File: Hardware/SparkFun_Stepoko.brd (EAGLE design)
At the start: 150 x 82 mm, 184 parts, among them J1 AVR ISP, Q1 16MHZ, Q2 100A/100V, U1 ATMEGA328, U2 CY7C65213, U3 74LVC1G04, U4 LM25011, U5 DRV8811, U6 74HC7014D, U7 7432SE, U8 DRV8811, U9 DRV8811

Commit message: found via hitting trace
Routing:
- net 5V: track 615.3 -> 613.5 mm
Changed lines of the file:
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@@
 <vertex x="15.24" y="37.084"/>
 </polygon>
-<via x="24.172" y="37.814" extent="1-16" drill="0.508" diameter="0.254"/>
-<via x="25.315" y="37.814" extent="1-16" drill="0.508" diameter="0.254"/>
+<via x="26.204" y="37.052" extent="1-16" drill="0.508" diameter="0.254"/>
+<via x="25.569" y="38.068" extent="1-16" drill="0.508" diameter="0.254"/>
 <via x="41.656" y="58.039" extent="1-16" drill="0.508"/>
 <via x="42.672" y="58.039" extent="1-16" drill="0.508"/>
@@
 <vertex x="101" y="78.73"/>
 </polygon>
-<wire x1="125" y1="39" x2="133" y2="39" width="0.4064" layer="16"/>
-<wire x1="133" y1="39" x2="135" y2="39" width="0.4064" layer="16"/>
-<via x="135" y="39" extent="1-16" drill="0.508" diameter="0.254"/>
-<via x="133" y="39" extent="1-16" drill="0.508" diameter="0.254"/>
+<wire x1="125" y1="39" x2="131.984" y2="39" width="0.4064" layer="16"/>
+<wire x1="131.984" y1="39" x2="133.222" y2="39" width="0.4064" layer="16"/>
+<via x="133.222" y="39" extent="1-16" drill="0.508" diameter="0.254"/>
+<via x="131.984" y="39" extent="1-16" drill="0.508" diameter="0.254"/>
 <wire x1="125" y1="30.826" x2="125" y2="36.068" width="0.4064" layer="16"/>
 <contactref element="C50" pad="2"/>

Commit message: corrected issues in github
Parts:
- D10, D14, D6: value YELLOW -> Yellow
- U10: value (none) -> +12v
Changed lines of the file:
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@@
 <layer number="113" name="IDFDebug" color="4" fill="1" visible="yes" active="yes"/>
 <layer number="116" name="Patch_BOT" color="9" fill="4" visible="yes" active="yes"/>
+<layer number="118" name="Rect_Pads" color="7" fill="1" visible="yes" active="yes"/>
 <layer number="121" name="_tsilk" color="7" fill="1" visible="yes" active="yes"/>
 <layer number="122" name="_bsilk" color="7" fill="1" visible="yes" active="yes"/>
@@
 <attribute name="PROD_ID" value="DIO-09912" x="21.5" y="76" size="1.778" layer="27" rot="R90" display="off"/>
 </element>
-<element name="D6" library="SparkFun-LED" package="LED-1206" value="YELLOW" x="29.5" y="76" rot="R90">
+<element name="D6" library="SparkFun-LED" package="LED-1206" value="Yellow" x="29.5" y="76" rot="R90">
 <attribute name="PROD_ID" value="DIO-09909" x="29.5" y="76" size="1.778" layer="27" rot="R90" display="off"/>
 </element>
@@
 <attribute name="PROD_ID" value="DIO-09912" x="40.08" y="70.92" size="1.778" layer="27" rot="R90" display="off"/>
 </element>
-<element name="D10" library="SparkFun-LED" package="LED-1206" value="YELLOW" x="43" y="76" rot="R90">
+<element name="D10" library="SparkFun-LED" package="LED-1206" value="Yellow" x="43" y="76" rot="R90">
 <attribute name="PROD_ID" value="DIO-09909" x="48.08" y="76" size="1.778" layer="27" rot="R90" display="off"/>
 </element>
@@
 <attribute name="PROD_ID" value="DIO-09912" x="53.58" y="70.92" size="1.778" layer="27" rot="R90" display="off"/>
 </element>
-<element name="D14" library="SparkFun-LED" package="LED-1206" value="YELLOW" x="56.5" y="76" rot="R90">
+<element name="D14" library="SparkFun-LED" package="LED-1206" value="Yellow" x="56.5" y="76" rot="R90">
 <attribute name="PROD_ID" value="DIO-09909" x="61.58" y="76" size="1.778" layer="27" rot="R90" display="off"/>
 </element>
@@
 <attribute name="PROD_ID" value="CAP-10547" x="113" y="59.5" size="1.016" layer="27" font="vector" ratio="15" rot="R180" display="off"/>
 </element>
-<element name="U10" library="SparkFun-PowerIC" package="TO-252" value="" x="78" y="67" rot="R90">
+<element name="U10" library="SparkFun-PowerIC" package="TO-252" value="+12v" x="78" y="67" rot="R90">
 <attribute name="PROD_ID" value="VREG-12370" x="78" y="67" size="1.778" layer="27" rot="R90" display="off"/>
 <attribute name="VALUE" value="+12v" x="78" y="67" size="1.778" layer="27" rot="R90" display="off"/>

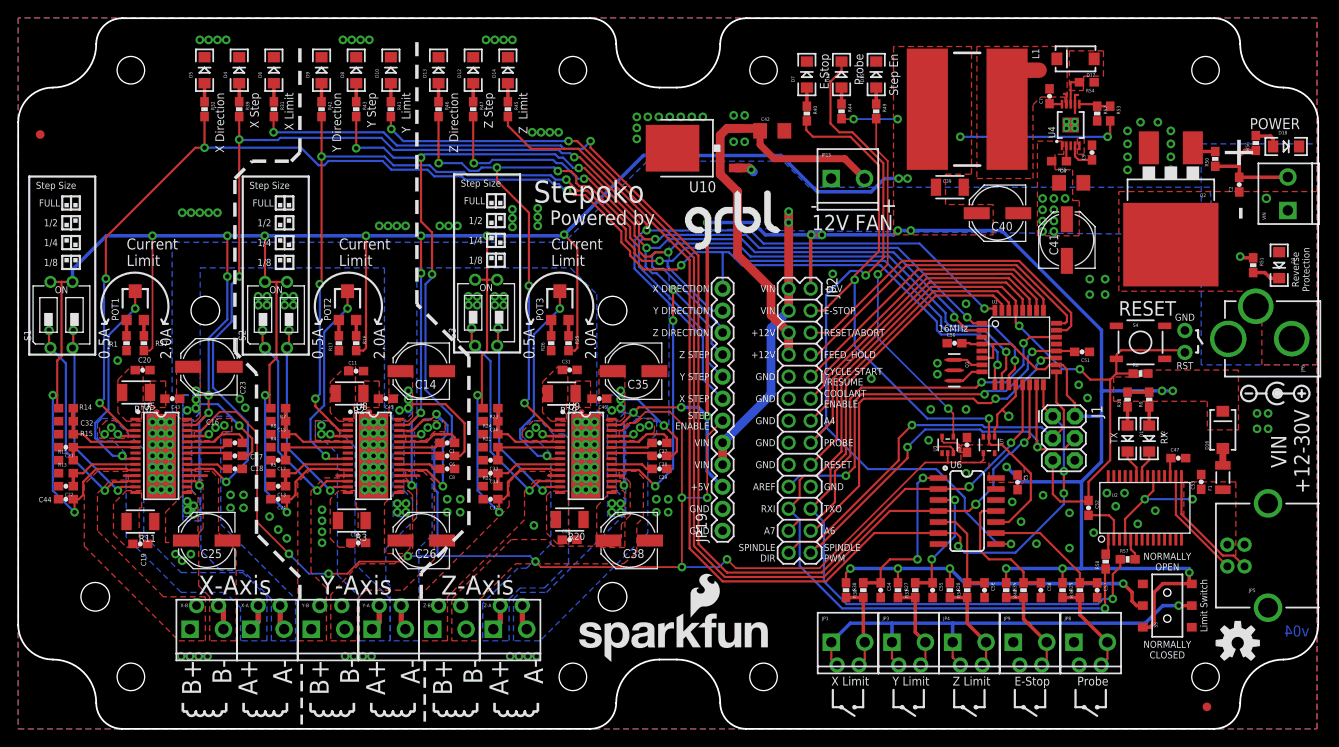
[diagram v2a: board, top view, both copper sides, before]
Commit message: Corrected Probe functionality and updated silk to better reflect limit switch functionality, moved Arduino table to better fit board layout
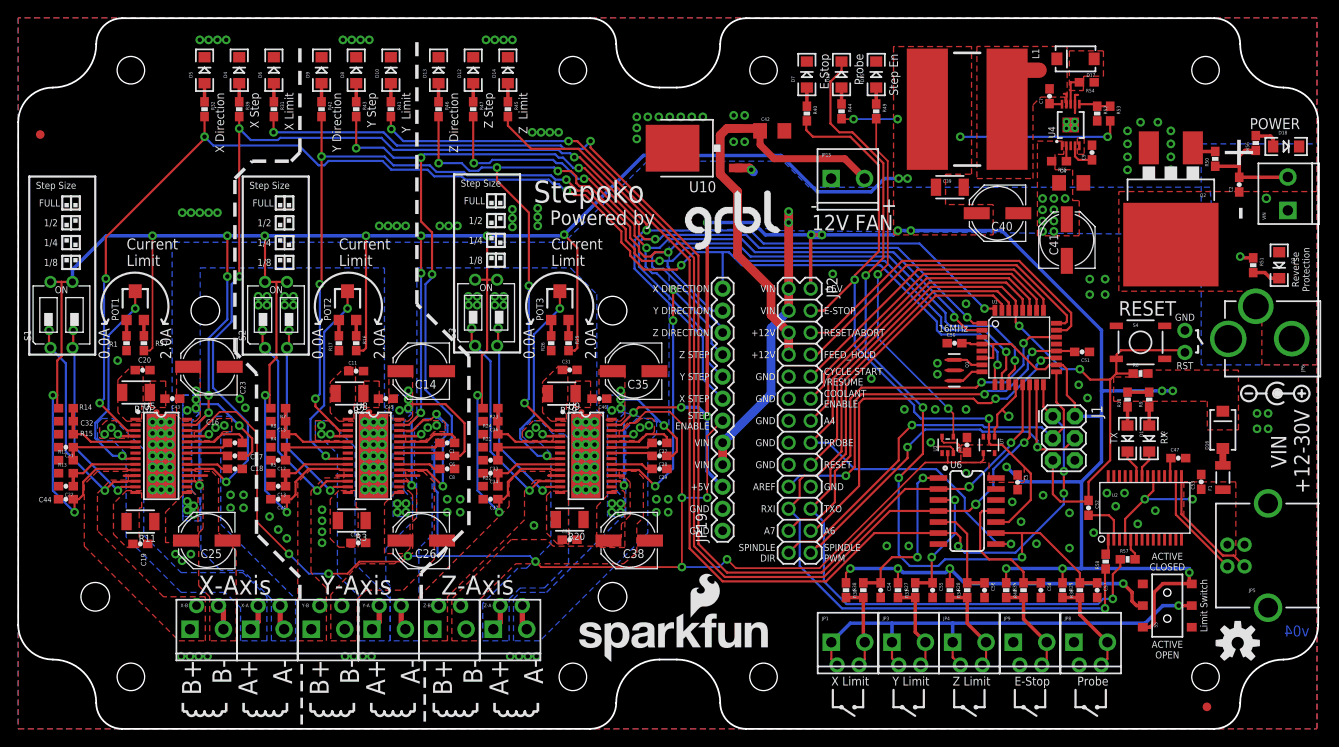
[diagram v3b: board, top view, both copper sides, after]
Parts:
- U2: value CY7C65213 -> FT232RLSSOP
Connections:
- net A5-PROBE: no longer D11.C
- net PROBE: now also D11.C
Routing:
- net PROBE: track 14.7 -> 98.3 mm, vias 0 -> 4
- net A5-PROBE: track 119.7 -> 67.6 mm, vias 2 -> 1
- net D2-STEP-X: track 171.7 -> 172.3 mm
- net GND: vias 149 -> 152
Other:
- board text added: "0.0A"
- board text added: "ACTIVE CLOSED"
- board text added: "ACTIVE OPEN"
- board text removed: "0.5A"
- board text removed: "NORMALLY CLOSED"
- board text removed: "NORMALLY OPEN"

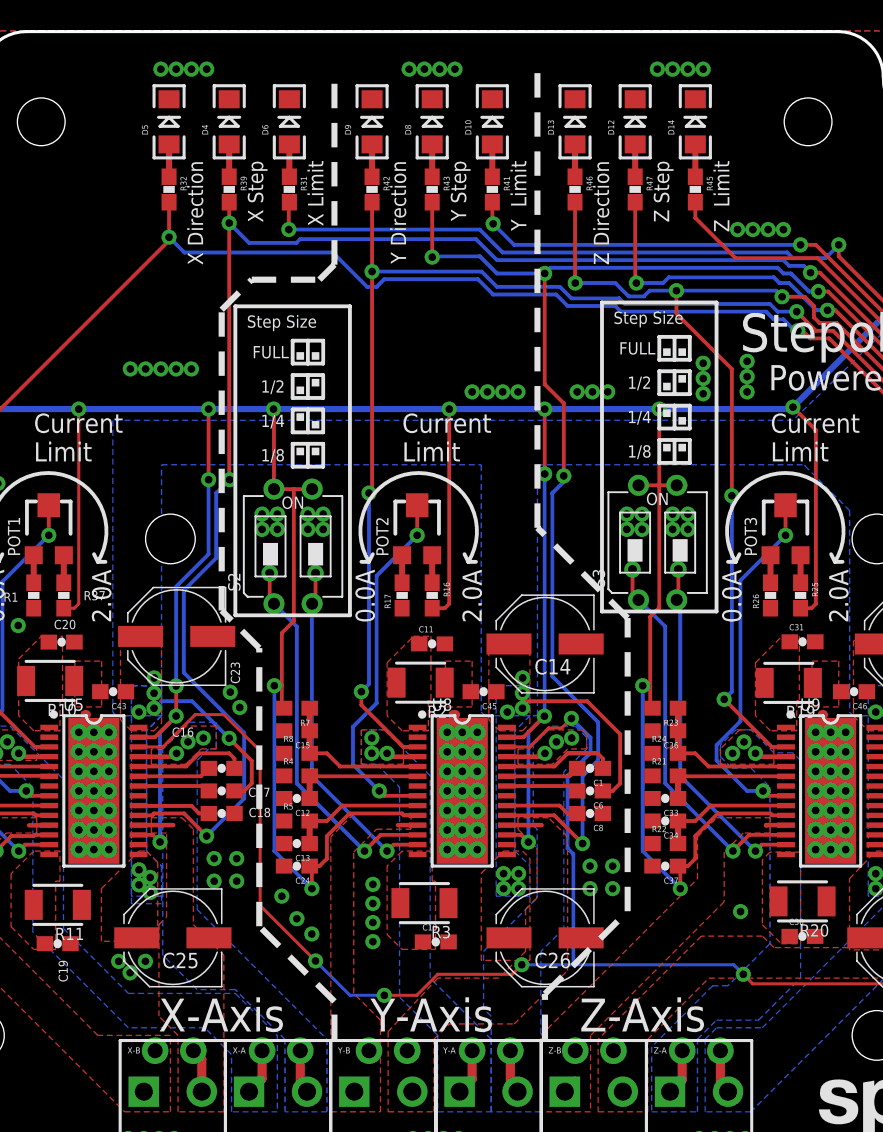
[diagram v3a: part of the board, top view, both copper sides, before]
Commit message: corrected issued from Design review. Opened up holes to prevent potential shorts, schematic cleanup.
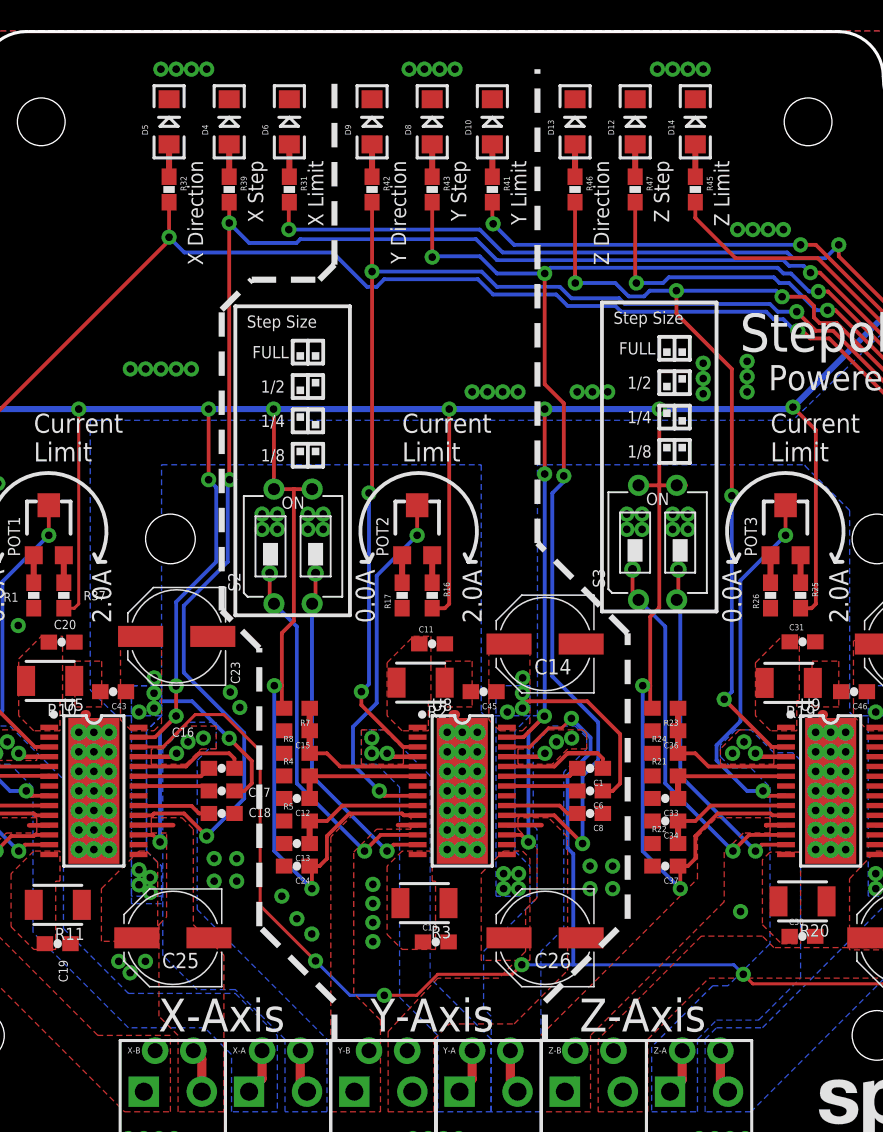
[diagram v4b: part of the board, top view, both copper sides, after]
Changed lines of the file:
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@@
 <setting verticaltext="up"/>
 </settings>
-<grid distance="0.01" unitdist="inch" unit="inch" style="lines" multiple="1" display="yes" altdistance="0.01" altunitdist="mm" altunit="mm"/>
+<grid distance="0.005" unitdist="inch" unit="inch" style="lines" multiple="1" display="yes" altdistance="0.01" altunitdist="mm" altunit="mm"/>
 <layers>
 <layer number="1" name="Top" color="4" fill="1" visible="yes" active="yes"/>
@@
 <text x="26.746" y="73.42" size="1.016" layer="21" font="vector" ratio="15" rot="R90" align="top-right">X Step</text>
 <text x="30.746" y="73.42" size="1.016" layer="21" font="vector" ratio="15" rot="R90" align="top-right">X Limit</text>
-<text x="44.246" y="73.42" size="1.016" layer="21" font="vector" ratio="15" rot="R90" align="top-right">Y  Limit</text>
-<text x="57.746" y="73.42" size="1.016" layer="21" font="vector" ratio="15" rot="R90" align="top-right">Z  Limit</text>
+<text x="44.246" y="73.42" size="1.016" layer="21" font="vector" ratio="15" rot="R90" align="top-right">Y Limit</text>
+<text x="57.746" y="73.42" size="1.016" layer="21" font="vector" ratio="15" rot="R90" align="top-right">Z Limit</text>
 <text x="40.246" y="73.42" size="1.016" layer="21" font="vector" ratio="15" rot="R90" align="top-right">Y Step</text>
 <text x="53.746" y="73.42" size="1.016" layer="21" font="vector" ratio="15" rot="R90" align="top-right">Z Step</text>
@@
 <wire x1="25" y1="43.5" x2="25" y2="63.5" width="0.4064" layer="21" style="longdash"/>
 <wire x1="32.5" y1="66.5" x2="32.5" y2="79.5" width="0.4064" layer="21" style="longdash"/>
-<wire x1="46.5" y1="15" x2="46.5" y2="18" width="0.4064" layer="21" style="longdash"/>
-<wire x1="46.5" y1="18" x2="52" y2="23.5" width="0.4064" layer="21" style="longdash"/>
-<wire x1="52" y1="23.5" x2="52" y2="43" width="0.4064" layer="21" style="longdash"/>
-<wire x1="52" y1="43" x2="46" y2="49" width="0.4064" layer="21" style="longdash"/>
-<wire x1="46" y1="49" x2="46" y2="79.5" width="0.4064" layer="21" style="longdash"/>
+<wire x1="46.5" y1="15" x2="46.5" y2="17.492" width="0.4064" layer="21" style="longdash"/>
+<wire x1="46.5" y1="17.492" x2="52" y2="22.992" width="0.4064" layer="21" style="longdash"/>
+<wire x1="52" y1="22.992" x2="52" y2="41.984" width="0.4064" layer="21" style="longdash"/>
+<wire x1="52" y1="41.984" x2="46" y2="47.984" width="0.4064" layer="21" style="longdash"/>
+<wire x1="46" y1="47.984" x2="46" y2="79.5" width="0.4064" layer="21" style="longdash"/>
 <text x="12.5" y="55" size="1.27" layer="21" font="vector" ratio="15" align="center-left">Current
 Limit</text>
@@
 <wire x1="67.564" y1="36.576" x2="67.564" y2="26.416" width="0.4064" layer="49"/>
 <wire x1="67.564" y1="26.416" x2="14.478" y2="26.416" width="0.4064" layer="49"/>
+<circle x="21.59" y="48.26" radius="2.794" width="0.254" layer="42"/>
+<circle x="68.58" y="15.24" radius="2.794" width="0.254" layer="42"/>
+<circle x="8.89" y="15.24" radius="2.794" width="0.254" layer="42"/>
+<circle x="8.89" y="15.24" radius="2.794" width="0.254" layer="41"/>
+<circle x="68.58" y="15.24" radius="2.794" width="0.254" layer="41"/>
+<circle x="68.58" y="48.26" radius="2.796884375" width="0.254" layer="41"/>
+<circle x="21.59" y="48.26" radius="2.794" width="0.254" layer="41"/>
+<circle x="68.58" y="48.26" radius="2.667" width="0.254" layer="42"/>
 </plain>
 <attributes>
@@
 <vertex x="72.596" y="65.5"/>
 <vertex x="62.992" y="56.15"/>
-<vertex x="17.762" y="56.15"/>
+<vertex x="16.256" y="56.15"/>
+<vertex x="16.256" y="38.227"/>
+<vertex x="17.653" y="36.83"/>
 </polygon>
 <wire x1="50.35" y1="31.5" x2="51" y2="31.5" width="0.254" layer="1"/>
@@
 <wire x1="26.5" y1="31" x2="26.5" y2="35.349" width="0.254" layer="16"/>
 <wire x1="26.5" y1="35.349" x2="22.479" y2="39.37" width="0.254" layer="16"/>
-<wire x1="22.479" y1="39.37" x2="22.479" y2="44.831" width="0.254" layer="16"/>
-<wire x1="22.479" y1="44.831" x2="24.638" y2="46.99" width="0.254" layer="16"/>
-<wire x1="24.638" y1="46.99" x2="24.638" y2="51.308" width="0.254" layer="16"/>
-<wire x1="24.638" y1="51.308" x2="25.527" y2="52.197" width="0.254" layer="16"/>
+<wire x1="22.479" y1="39.37" x2="22.479" y2="43.815" width="0.254" layer="16"/>
+<wire x1="22.479" y1="43.815" x2="25.4" y2="46.736" width="0.254" layer="16"/>
+<wire x1="25.4" y1="46.736" x2="25.4" y2="52.07" width="0.254" layer="16"/>
+<wire x1="25.4" y1="52.07" x2="25.527" y2="52.197" width="0.254" layer="16"/>
 <via x="25.527" y="52.197" extent="1-16" drill="0.508"/>
 <wire x1="64.159" y1="65.968" x2="63.706" y2="66.421" width="0.254" layer="16"/>
@@
 <wire x1="6.262" y1="52.998" x2="10.16" y2="56.896" width="0.4064" layer="16"/>
 <wire x1="6.262" y1="51.572" x2="5" y2="51.572" width="0.254" layer="1"/>
-<wire x1="21.971" y1="38.481" x2="21.971" y2="45.085" width="0.254" layer="16"/>
-<wire x1="21.971" y1="45.085" x2="24.13" y2="47.244" width="0.254" layer="16"/>
-<wire x1="24.13" y1="47.244" x2="24.13" y2="52.197" width="0.254" layer="16"/>
+<wire x1="21.971" y1="38.481" x2="21.971" y2="44.069" width="0.254" layer="16"/>
+<wire x1="21.971" y1="44.069" x2="24.638" y2="46.736" width="0.254" layer="16"/>
 <wire x1="24.13" y1="52.197" x2="24.13" y2="56.896" width="0.254" layer="1"/>
 <via x="24.13" y="56.896" extent="1-16" drill="0.508"/>
@@
 <wire x1="54.102" y1="51.826" x2="52.722" y2="51.826" width="0.254" layer="1"/>
 <wire x1="64.516" y1="55.499" x2="62.992" y2="57.023" width="0.254" layer="1"/>
+<wire x1="24.638" y1="46.736" x2="24.638" y2="51.689" width="0.254" layer="16"/>
+<wire x1="24.638" y1="51.689" x2="24.13" y2="52.197" width="0.254" layer="16"/>
 </signal>
 <signal name="ESTOP-LOGIC">

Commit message: updated version number
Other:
- board text added: "v10"
- board text removed: "v04"
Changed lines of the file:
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@@
 <board>
 <plain>
-<text x="148.99" y="10.66" size="1.27" layer="16" font="vector" ratio="20" rot="MR0">v04</text>
+<text x="148.99" y="10.66" size="1.27" layer="16" font="vector" ratio="20" rot="MR0">v10</text>
 <text x="149" y="32" size="1.778" layer="21" font="vector" ratio="15" rot="R90" align="bottom-center">VIN
 +12-30V</text>
